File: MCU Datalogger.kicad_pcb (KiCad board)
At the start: 2 copper layers, 29 parts, among them J1 Conn_01x04_Pin, J2 Conn_01x04_Pin, J3 Conn_01x09, J4 Conn_02x03_Odd_Even, U1 24LC1025, U2 24LC1025, U3 DS1337S_T_R, U4 ATMEGA328P-AN, Y1 32.768 KHz, Y2 16 MHz

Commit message: add most of the routes
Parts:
- moved J3 96.7 mm to (144.7, 146.2), turned to 90 degrees
- moved BT1 91.5 mm to (140.1, 127.9)
- moved U3 82.7 mm to (147.9, 138.2)
- moved J2 81.4 mm to (169.9, 146.2), turned to 90 degrees
- moved Y1 80.0 mm to (139.8, 138.9), turned to 90 degrees
- moved C3 73.1 mm to (156.2, 120.1)
- moved U1 73.0 mm to (147.6, 122.0)
- moved U2 72.9 mm to (147.4, 130.0)
- moved H2 69.6 mm to (139.7, 146.2)
- moved C2 68.2 mm to (160.5, 120.1)
- moved H1 67.3 mm to (139.7, 120.5)
- moved C5 66.5 mm to (165.2, 120.1)
- moved R7 66.2 mm to (145.9, 142.6)
- moved D2 65.0 mm to (170.6, 120.3)
- moved R6 62.3 mm to (150.1, 142.6)
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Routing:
- net /SCK: track 0.00 -> 85.1 mm, vias 0 -> 2
- net /Vcc: track 0.00 -> 73.8 mm, vias 0 -> 1
- net /SDA: track 0.00 -> 66.0 mm, vias 0 -> 2
- net GND: track 0.00 -> 54.8 mm, vias 0 -> 6
- net Net-(BT1-+): track 0.00 -> 34.5 mm, vias 0 -> 1
- net /TX: track 0.00 -> 32.5 mm, vias 0 -> 1
- net /RX: track 0.00 -> 30.1 mm, vias 0 -> 1
- net /D3: track 0.00 -> 27.7 mm
- net /MOSI: track 0.00 -> 27.4 mm
- net /D2: track 0.00 -> 26.5 mm, vias 0 -> 1
- net Net-(U4-PB6): track 0.00 -> 25.8 mm
- net /MISO: track 0.00 -> 21.9 mm, vias 0 -> 1
- net Net-(U4-AREF): track 0.00 -> 18.3 mm, vias 0 -> 2
- net Net-(U4-PB7): track 0.00 -> 12.8 mm
- net Net-(U3-X2): track 0.00 -> 8.26 mm
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
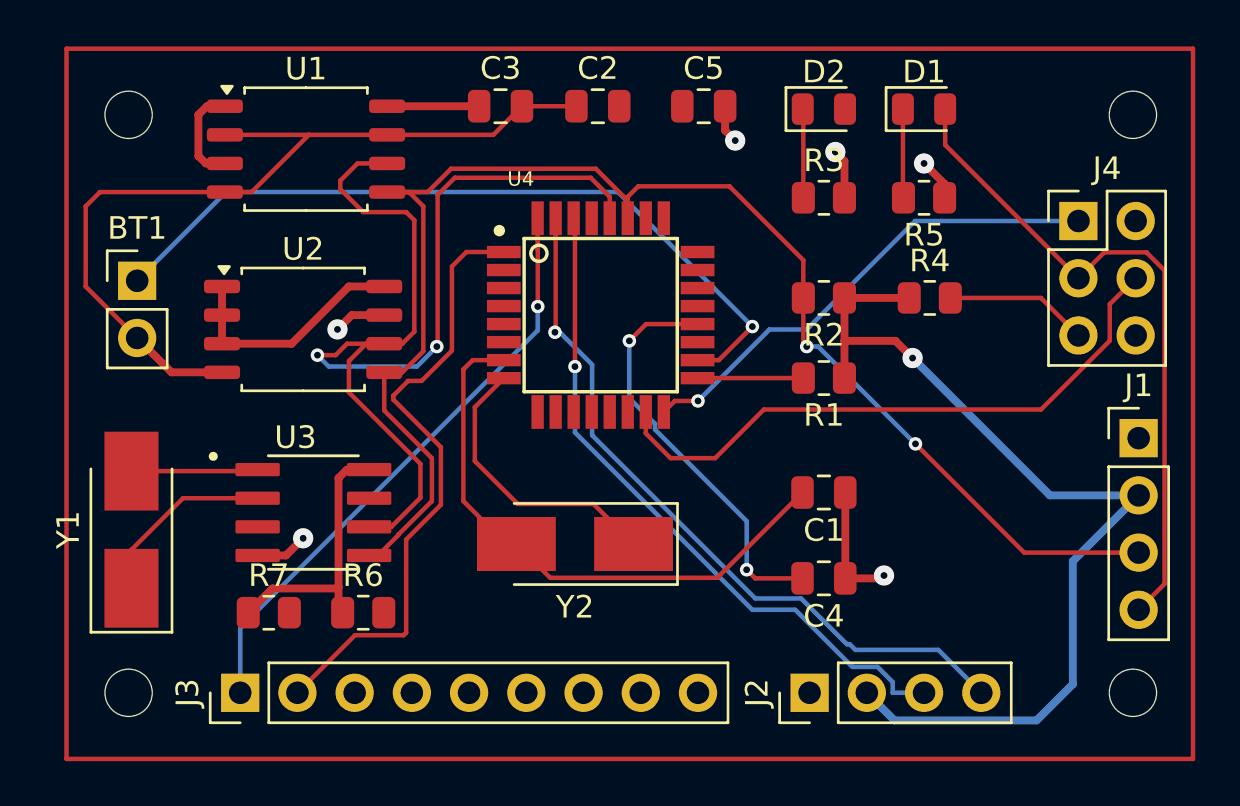
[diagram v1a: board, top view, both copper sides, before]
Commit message: fix some routes and add copper fills
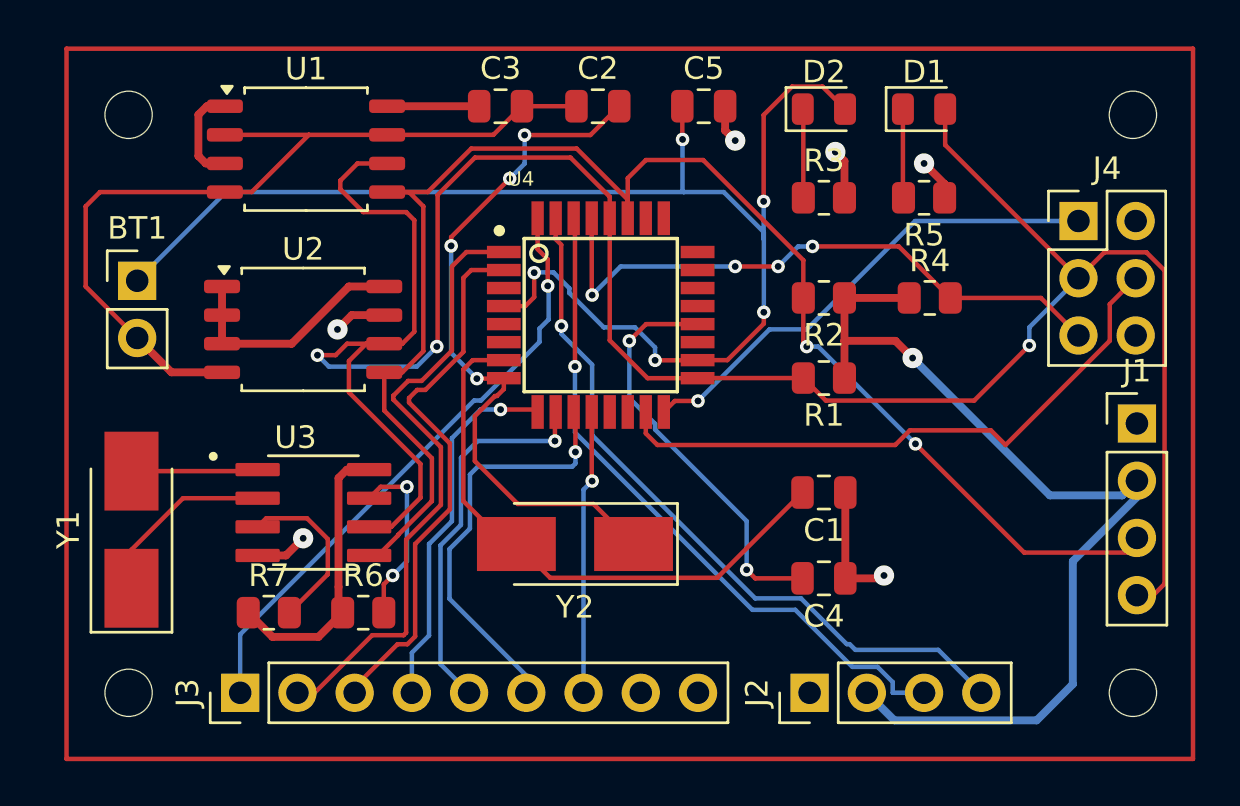
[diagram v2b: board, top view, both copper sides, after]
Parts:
- moved J1 0.65 mm to (184.5, 134.2)
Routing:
- net Net-(BT1-+): track 34.5 -> 63.7 mm, vias 1 -> 5
- net /SCK: track 85.1 -> 111.2 mm, vias 2 -> 3
- net /D4: track 0.00 -> 24.3 mm
- net /RESET: track 6.38 -> 27.5 mm, vias 0 -> 4
- net /D7: track 0.00 -> 18.8 mm, vias 0 -> 1
- net Net-(U4-PB7): track 12.8 -> 31.4 mm, vias 0 -> 4
- net /D6: track 0.00 -> 17.1 mm, vias 0 -> 1
- net /D5: track 0.00 -> 16.4 mm, vias 0 -> 1
- net /D8: track 0.00 -> 12.6 mm, vias 0 -> 1
- net Net-(U3-SQW/~INT): track 0.00 -> 7.90 mm, vias 0 -> 2
- net Net-(U3-~{INTA}): track 0.00 -> 7.63 mm
- net /SDA: track 66.0 -> 68.2 mm
- net /Vcc: track 73.8 -> 75.2 mm
- net /D2: track 26.5 -> 27.1 mm

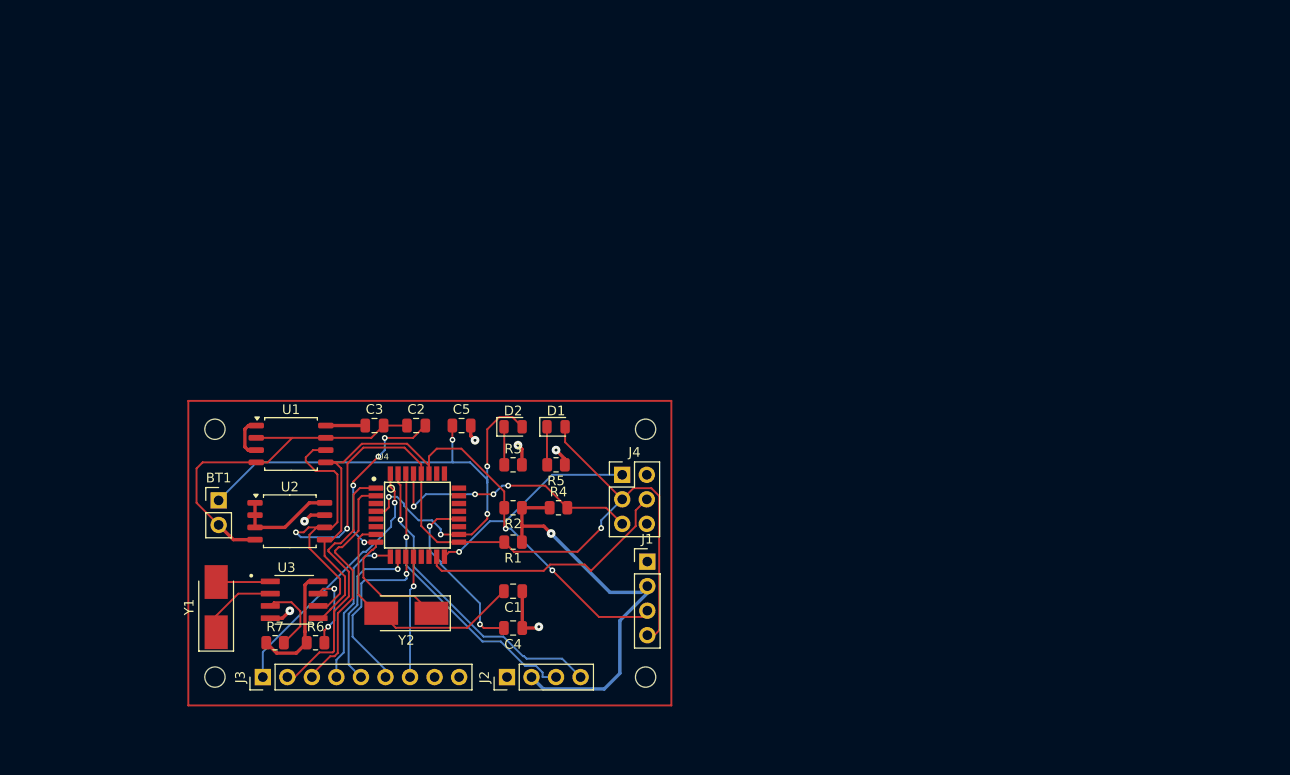
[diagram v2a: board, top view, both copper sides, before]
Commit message: finish the 2-layer pcb
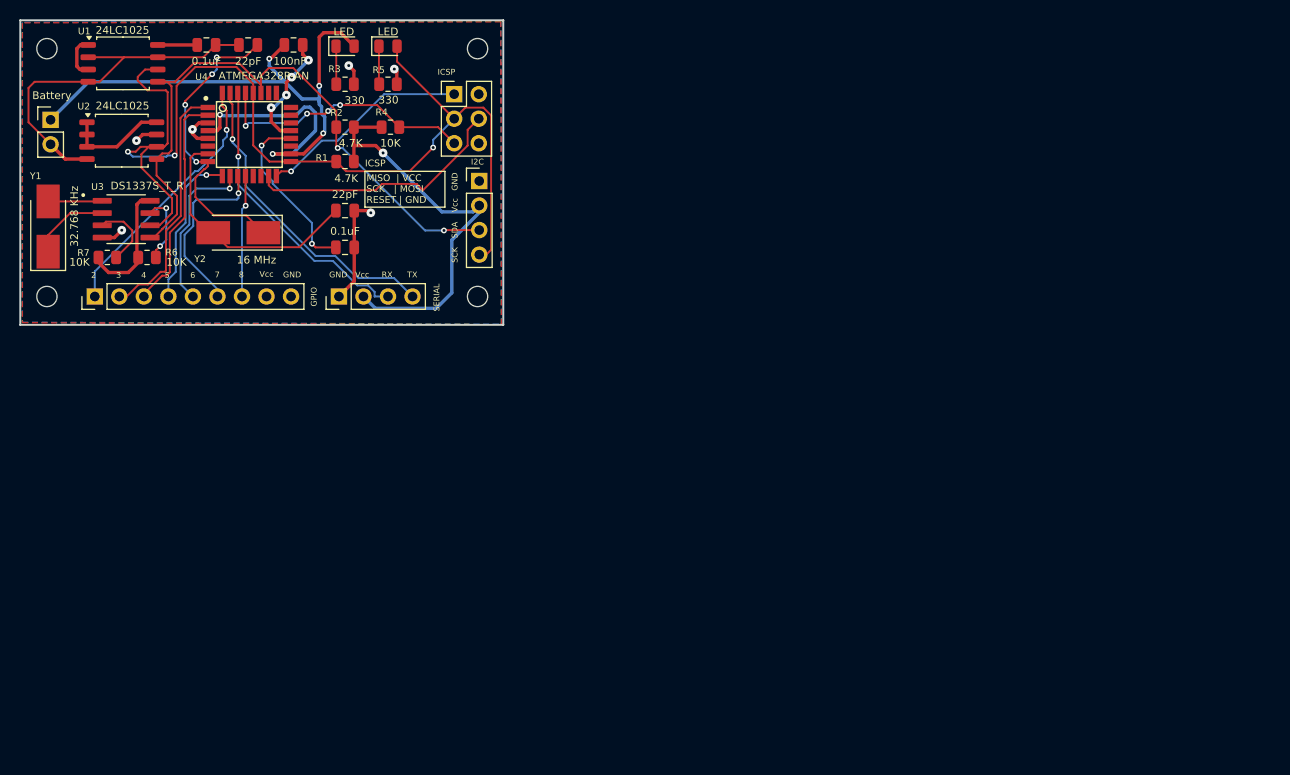
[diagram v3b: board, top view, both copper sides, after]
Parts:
- moved R6 43.5 mm to (132.7, 102.7)
- moved R7 43.5 mm to (128.6, 102.7)
- moved C1 43.1 mm to (153.2, 97.9)
- moved C4 43.1 mm to (153.2, 101.7)
- moved D1 43.1 mm to (157.6, 80.9)
- moved D2 43.1 mm to (153.2, 80.9)
- moved J1 43.1 mm to (167.1, 94.8)
- moved R2 43.1 mm to (153.2, 89.3)
- moved R3 43.1 mm to (153.2, 84.8)
- moved R4 43.1 mm to (157.9, 89.3)
- moved R5 43.1 mm to (157.6, 84.8)
- moved U4 43.1 mm to (143.3, 90.0)
- moved Y2 43.1 mm to (142.1, 100.2)
- moved C2 43.1 mm to (143.1, 80.7)
- moved C3 43.1 mm to (138.8, 80.7)
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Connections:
- BT1 pad 1: Net-(BT1-+) -> /Vcc
- C5 pad 1: Net-(BT1-+) -> /Vcc
- D2 pad 2: Net-(BT1-+) -> /Vcc
- U4 pad 18: Net-(BT1-+) -> /Vcc
- U4 pad 4: Net-(BT1-+) -> /Vcc
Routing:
- net /Vcc: track 75.2 -> 152.8 mm, vias 1 -> 6
- net Net-(BT1-+): track 63.7 -> 0.00 mm, vias 5 -> 0
- net GND: track 54.8 -> 75.0 mm, vias 6 -> 10
- net /D3: track 27.7 -> 25.7 mm
- net /D4: track 24.3 -> 23.0 mm
- net Net-(U3-SQW/~INT): track 7.90 -> 8.67 mm
- net /SDA: track 68.2 -> 67.7 mm
- added copper zone on F.Cu, net /Vcc
- added copper zone on B.Cu, net GND
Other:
- board outline added: 50 x 31.5 mm
- board text added: "2"
- board text added: "3"
- board text added: "4"
- board text added: "5"
- board text added: "6"
- board text added: "7"
- board text added: "8"
- board text added: "GND"
- board text added: "GPIO"
- board text added: "I2C"
- board text added: "ICSP"
- board text added: "MISO | VCC SCK | MOSI RESET | GND"
- board text added: "RX"
- board text added: "SCK"
- board text added: "SDA"
- board text added: "SERIAL"
- board text added: "TX"
- board text added: "Vcc"

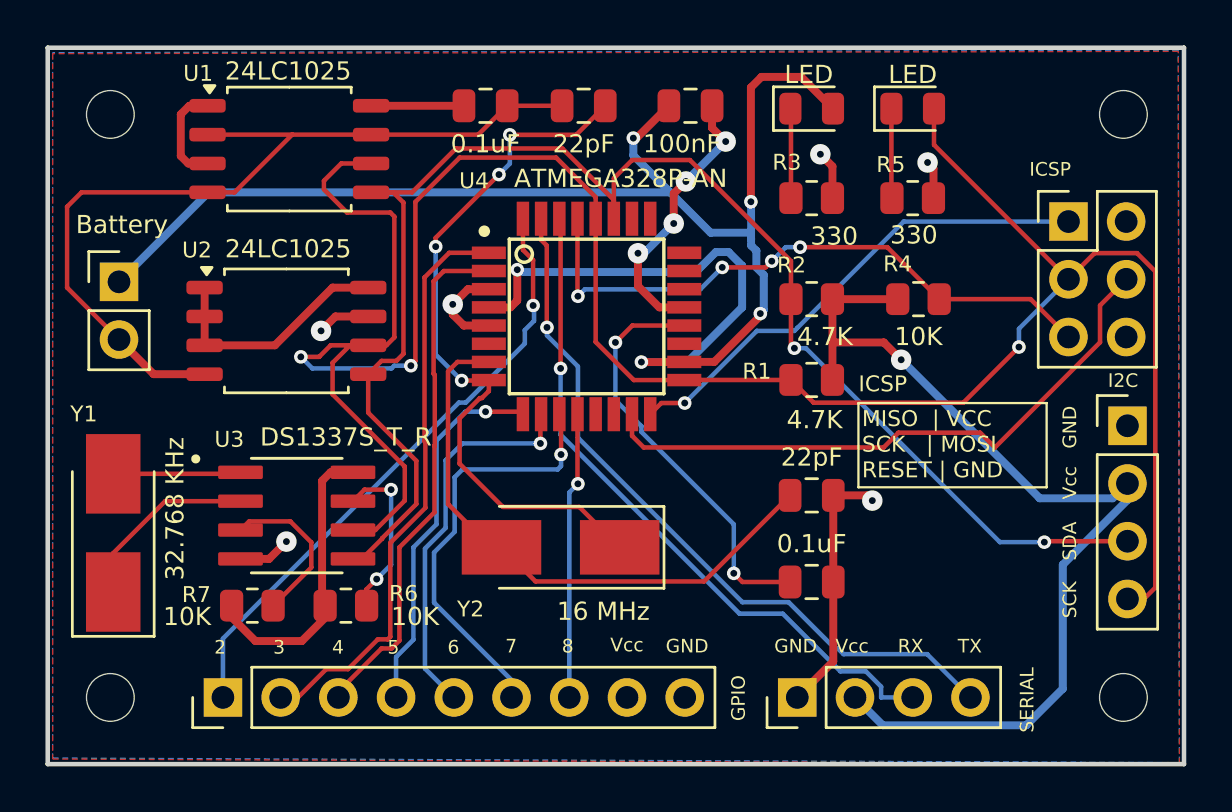
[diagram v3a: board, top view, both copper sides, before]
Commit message: update routes for 4-layer pcb
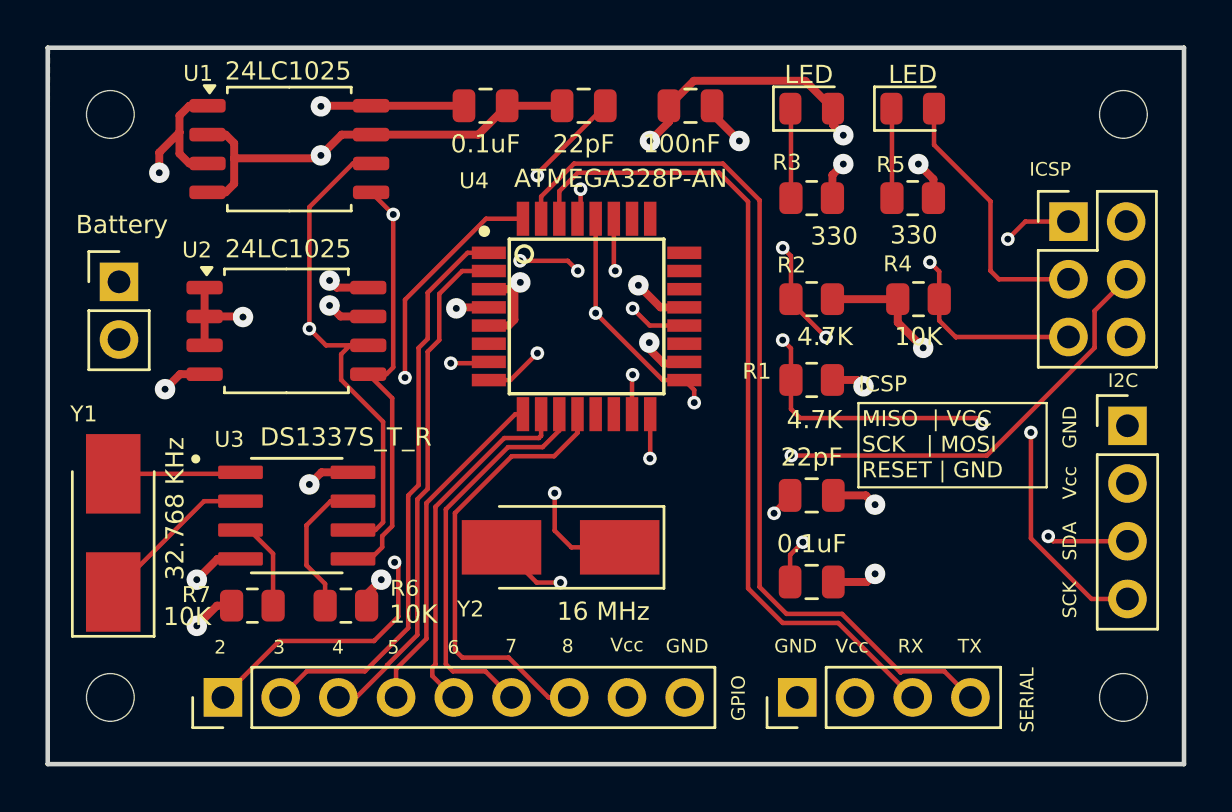
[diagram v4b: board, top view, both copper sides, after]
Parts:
- turned R6 to 180 degrees
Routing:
- net /Vcc: track 152.8 -> 54.2 mm, vias 6 -> 13
- net GND: track 75.0 -> 43.2 mm, vias 10 -> 11
- net /SCK: track 111.2 -> 94.5 mm, vias 3 -> 6
- net /TX: track 32.3 -> 40.2 mm, vias 1 -> 0
- net /D8: track 12.6 -> 19.6 mm, vias 1 -> 0
- net /RX: track 30.1 -> 36.6 mm, vias 1 -> 0
- net /SDA: track 67.7 -> 61.7 mm, vias 2 -> 7
- net Net-(U4-PB7): track 31.4 -> 26.3 mm, vias 4 -> 3
- net Net-(U4-AREF): track 18.3 -> 21.6 mm
- net Net-(U3-~{INTA}): track 7.14 -> 4.15 mm
- net /D2: track 27.1 -> 30.1 mm, vias 1 -> 2
- net /MISO: track 21.9 -> 24.7 mm, vias 1 -> 2
- net Net-(U4-PB6): track 25.8 -> 28.3 mm, vias 0 -> 3
- net Net-(U3-SQW/~INT): track 8.67 -> 6.76 mm, vias 2 -> 0
- net /MOSI: track 27.5 -> 29.1 mm, vias 0 -> 2
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- added copper zone on In2.Cu, net /Vcc
- removed copper zone on F.Cu, net /Vcc
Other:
- copper layers 2 -> 4

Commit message: fix pcb after schematic bug (4-layer pcb)
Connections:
- J1 pad 4: /SCK -> /SCL
- R1 pad 2: /SCK -> /SCL
- U1 pad 6: /SCK -> /SCL
- U2 pad 6: /SCK -> /SCL
- U3 pad 6: /SCK -> /SCL
- U4 pad 28: /SCK -> /SCL
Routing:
- net /SCL: track 0.00 -> 82.5 mm, vias 0 -> 6
- net /SCK: track 94.5 -> 33.9 mm, vias 6 -> 3
